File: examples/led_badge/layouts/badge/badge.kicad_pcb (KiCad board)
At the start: 2 copper layers, 56.3 x 38 mm, 237 parts

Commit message: layout tidy up
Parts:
- added U6: , MOLEX_532610271:CONN-SMD_532610271, F.Cu at (121.2, 103.0)
- moved B1 9.35 mm to (96.6, 100.2)
- moved R9 1.01 mm to (115.2, 114.0)
- moved R10 1.01 mm to (115.1, 111.0)
- moved USB1 1.01 mm to (119.7, 112.8)
- moved C111 0.32 mm to (107.2, 103.9)
- moved C4 0.32 mm to (116.1, 103.7)
- moved L1 0.32 mm to (112.7, 107.6)
- moved U2 0.32 mm to (112.6, 104.1)
- moved R1 0.32 mm to (107.9, 107.1)
- moved C110 0.32 mm to (109.0, 103.9)
- moved C112 0.32 mm to (115.3, 107.1)
- moved C3 0.32 mm to (117.9, 103.7)
- moved R2 0.32 mm to (109.2, 107.0)
- moved R3 0.32 mm to (114.5, 100.9)
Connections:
- LED1 pad 4: led_grid-line-0 -> line-11
- LED10 pad 2: led_grid-line-2 -> led_grid-line-1
- LED100 pad 2: led_grid-line-1 -> led_grid-line-0
- LED11 pad 4: led_grid-line-2 -> led_grid-line-1
- LED20 pad 2: led_grid-line-3 -> led_grid-line-2
- LED21 pad 4: led_grid-line-3 -> led_grid-line-2
- LED30 pad 2: led_grid-line-4 -> led_grid-line-3
- LED31 pad 4: led_grid-line-4 -> led_grid-line-3
- LED40 pad 2: led_grid-line-5 -> led_grid-line-4
- LED41 pad 4: led_grid-line-5 -> led_grid-line-4
- LED50 pad 2: led_grid-line-6 -> led_grid-line-5
- LED51 pad 4: led_grid-line-6 -> led_grid-line-5
- LED60 pad 2: led_grid-line-7 -> led_grid-line-6
- LED61 pad 4: led_grid-line-7 -> led_grid-line-6
- LED70 pad 2: led_grid-line-8 -> led_grid-line-7
- LED71 pad 4: led_grid-line-8 -> led_grid-line-7
- LED80 pad 2: led_grid-line-9 -> led_grid-line-8
- LED81 pad 4: led_grid-line-9 -> led_grid-line-8
- LED90 pad 2: led_grid-line-10 -> led_grid-line-9
- LED91 pad 4: led_grid-line-10 -> led_grid-line-9
- U3 pad : (no net) -> mic.package.footprint.pins[0].net-net
- USB1 pad : (no net) -> usb_c.conn.footprint.pins[0].net-net
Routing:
- net led_grid-line-10: track 41.6 -> 0.00 mm, vias 2 -> 0
- net led_grid-line-1: track 0.00 -> 41.3 mm, vias 0 -> 2
- net line-11: track 0.00 -> 0.73 mm, vias 0 -> 1

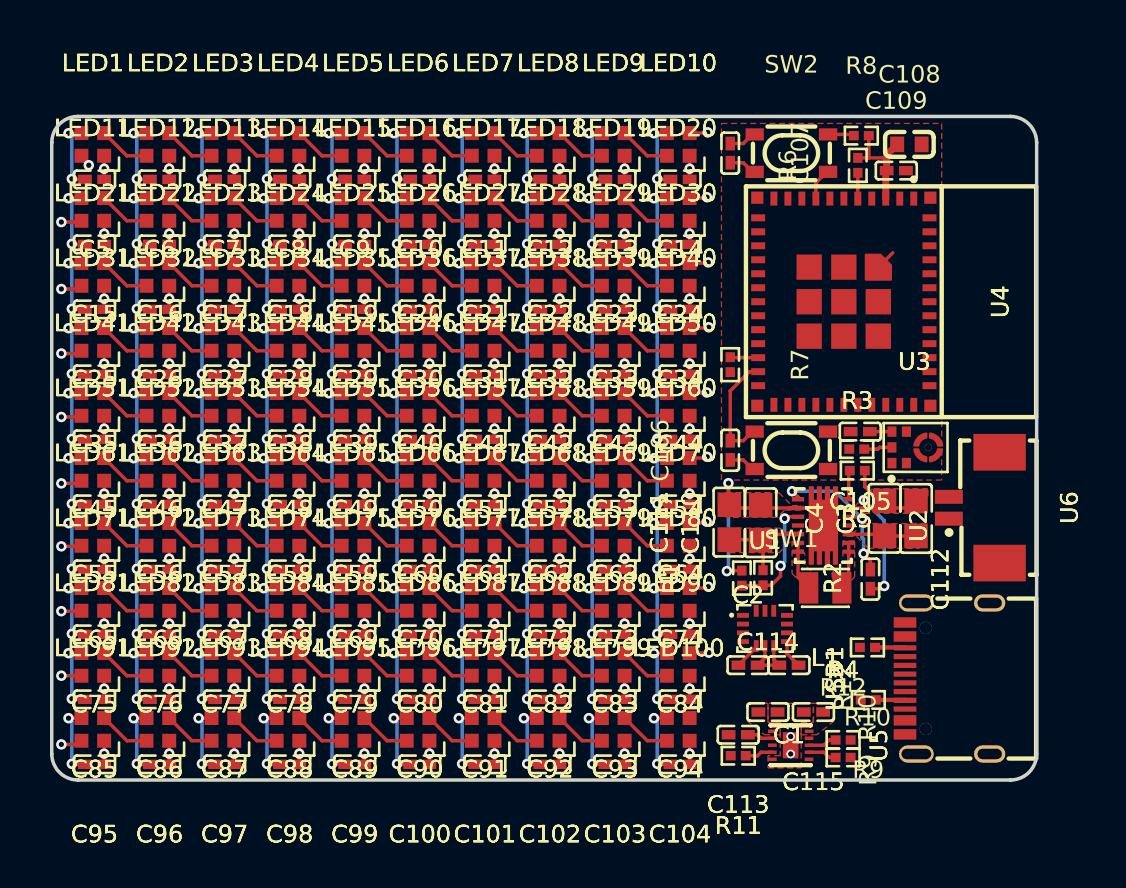
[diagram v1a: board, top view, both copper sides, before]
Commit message: fix 3d models
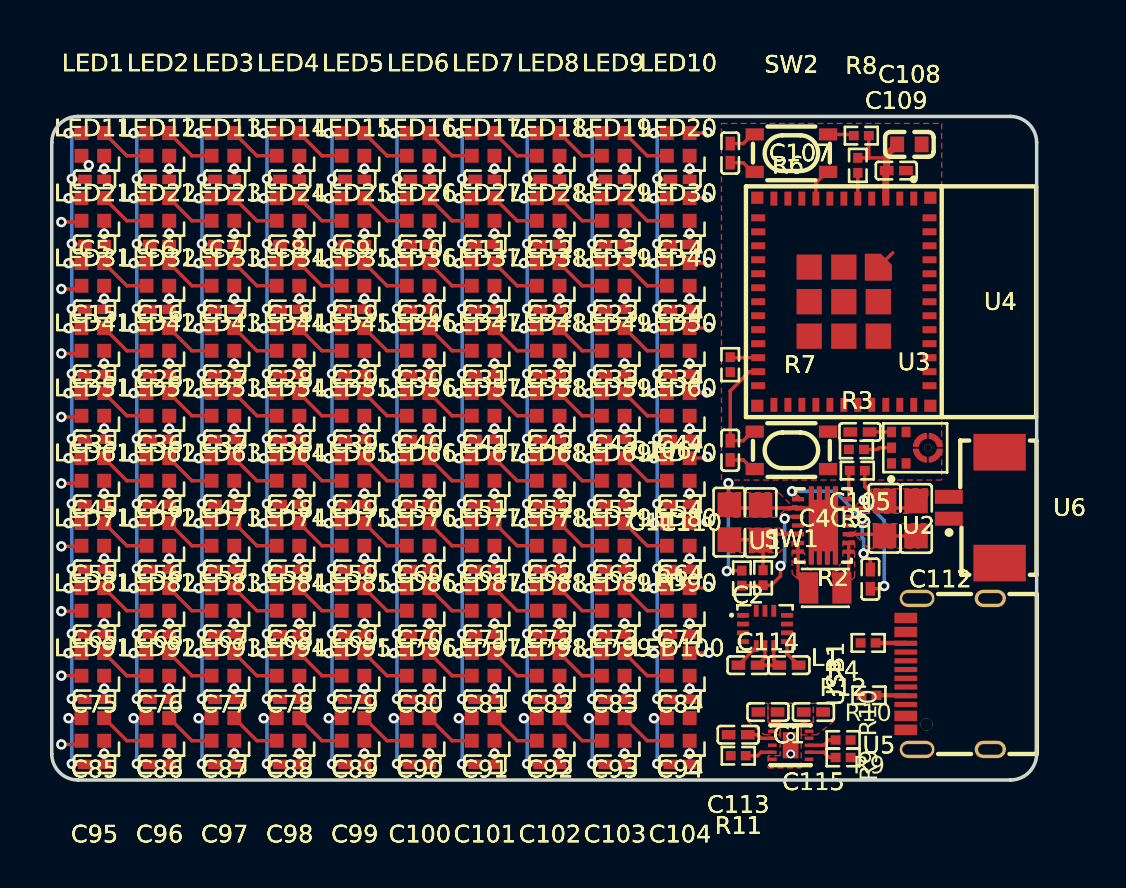
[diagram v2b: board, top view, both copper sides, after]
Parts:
- moved R10 0.26 mm to (115.2, 110.8)
- moved R9 0.26 mm to (115.2, 113.8)
- moved USB1 0.26 mm to (119.7, 112.5)
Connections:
- net mic.package.footprint.pins[0].net-net renamed microphone.package.footprint.pins[0].net-net
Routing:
- removed copper zone on F.Cu, net IN

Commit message: almost complete layout
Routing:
- net line-11: track 0.73 -> 50.8 mm, vias 1 -> 2
- net BAT: track 1.48 -> 29.9 mm, vias 0 -> 4
- net -hv: track 3.90 -> 19.5 mm
- net line-4: track 0.00 -> 15.4 mm, vias 0 -> 2
- net IN: track 0.00 -> 15.3 mm
- net line-3: track 0.00 -> 14.8 mm, vias 0 -> 2
- net hv: track 151.6 -> 164.7 mm, vias 100 -> 112
- net line-5: track 1.62 -> 13.4 mm, vias 0 -> 2
- net gnd: track 453.0 -> 460.1 mm, vias 206 -> 213
- net output-1: track 6.52 -> 10.7 mm
- net output-0: track 3.48 -> 7.68 mm
- net input: track 3.11 -> 7.31 mm
- added copper zone on B.Cu, net gnd
- added copper zone on In1.Cu, net gnd
- added copper zone on In2.Cu, net gnd
- added copper zone on B.Cu, net hv
- added copper zone on In1.Cu, net hv
- added copper zone on In2.Cu, net hv
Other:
- board size 56.3 x 38 mm -> 56.3 x 39 mm
- copper layers 2 -> 4

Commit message: layout ready for final review
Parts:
- added R13: 4.7kΩ ±1% 62.5mW, UNI_ROYAL_0402WGF4701TCE:R0402, F.Cu at (107.2, 90.8)
- added R14: 4.7kΩ ±1% 62.5mW, UNI_ROYAL_0402WGF4701TCE:R0402, F.Cu at (107.2, 92.8)
- added R15: 10kΩ ±1% 62.5mW, UNI_ROYAL_0402WGF1002TCE:R0402, F.Cu at (114.2, 82.2)
- moved R6 23.2 mm to (115.9, 106.6), turned to -90 degrees
- moved R8 15.1 mm to (107.2, 94.8), turned to -90 degrees
- moved R7 15.1 mm to (115.3, 82.2), turned to 90 degrees
- moved B1 2.20 mm to (94.6, 99.2)
- moved C112 0.39 mm to (114.9, 107.2)
- moved U6 0.20 mm to (121.0, 103.0)
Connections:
- net -hv renamed power_sys
- net BAT renamed power_batt
- net line-10 renamed micro-line-6
- net line-12 renamed micro-line-7
- net line-6 renamed micro-line-3
- net line-8 renamed micro-line-4
- net line-9 renamed micro-line-5
- net micro.esp32_module.package.footprint.pins[16].net-net renamed micro.esp32_c3.package.footprint.pins[16].net-net
- net micro.esp32_module.package.footprint.pins[17].net-net renamed micro.esp32_c3.package.footprint.pins[17].net-net
- net micro.esp32_module.package.footprint.pins[1].net-net renamed micro.esp32_c3.package.footprint.pins[1].net-net
- net micro.esp32_module.package.footprint.pins[20].net-net renamed micro.esp32_c3.package.footprint.pins[20].net-net
- net micro.esp32_module.package.footprint.pins[21].net-net renamed micro.esp32_c3.package.footprint.pins[21].net-net
- net micro.esp32_module.package.footprint.pins[25].net-net renamed micro.esp32_c3.package.footprint.pins[25].net-net
- net micro.esp32_module.package.footprint.pins[26].net-net renamed micro.esp32_c3.package.footprint.pins[26].net-net
- net micro.esp32_module.package.footprint.pins[27].net-net renamed micro.esp32_c3.package.footprint.pins[27].net-net
- net micro.esp32_module.package.footprint.pins[28].net-net renamed micro.esp32_c3.package.footprint.pins[28].net-net
- net micro.esp32_module.package.footprint.pins[33].net-net renamed micro.esp32_c3.package.footprint.pins[33].net-net
- net micro.esp32_module.package.footprint.pins[50].net-net renamed micro.esp32_c3.package.footprint.pins[50].net-net
- net micro.esp32_module.package.footprint.pins[52].net-net renamed micro.esp32_c3.package.footprint.pins[52].net-net
- net micro.esp32_module.package.footprint.pins[6].net-net renamed micro.esp32_c3.package.footprint.pins[6].net-net
- net micro.esp32_module.package.footprint.pins[8].net-net renamed micro.esp32_c3.package.footprint.pins[8].net-net
- C1 pad 1: hv -> power_3v3
- C10 pad 1: hv -> power_3v3
- C100 pad 1: hv -> power_3v3
- C101 pad 1: hv -> power_3v3
- C102 pad 1: hv -> power_3v3
- C103 pad 1: hv -> power_3v3
- C104 pad 1: hv -> power_3v3
- C105 pad 1: hv -> power_3v3
- C106 pad 2: output-1 -> output-0
- C107 pad 1: input -> gnd
- C107 pad 2: output-0 -> output-1
- C108 pad 1: hv -> power_3v3
- C109 pad 1: hv -> power_3v3
- C11 pad 1: hv -> power_3v3
- C110 pad 1: hv -> power_3v3
- C111 pad 1: hv -> power_3v3
- C115 pad 1: IN -> usb_power
- C12 pad 1: hv -> power_3v3
- C13 pad 1: hv -> power_3v3
- C14 pad 1: hv -> power_3v3
- C15 pad 1: hv -> power_3v3
- C16 pad 1: hv -> power_3v3
- C17 pad 1: hv -> power_3v3
- C18 pad 1: hv -> power_3v3
- C19 pad 1: hv -> power_3v3
- C2 pad 1: hv -> power_3v3
- C20 pad 1: hv -> power_3v3
- C21 pad 1: hv -> power_3v3
- C22 pad 1: hv -> power_3v3
- C23 pad 1: hv -> power_3v3
- C24 pad 1: hv -> power_3v3
- C25 pad 1: hv -> power_3v3
- C26 pad 1: hv -> power_3v3
- C27 pad 1: hv -> power_3v3
- C28 pad 1: hv -> power_3v3
- C29 pad 1: hv -> power_3v3
- C30 pad 1: hv -> power_3v3
- C31 pad 1: hv -> power_3v3
- C32 pad 1: hv -> power_3v3
- C33 pad 1: hv -> power_3v3
- C34 pad 1: hv -> power_3v3
- C35 pad 1: hv -> power_3v3
- C36 pad 1: hv -> power_3v3
- C37 pad 1: hv -> power_3v3
- C38 pad 1: hv -> power_3v3
- C39 pad 1: hv -> power_3v3
- C40 pad 1: hv -> power_3v3
- C41 pad 1: hv -> power_3v3
- C42 pad 1: hv -> power_3v3
- C43 pad 1: hv -> power_3v3
- C44 pad 1: hv -> power_3v3
- C45 pad 1: hv -> power_3v3
- C46 pad 1: hv -> power_3v3
- C47 pad 1: hv -> power_3v3
- C48 pad 1: hv -> power_3v3
- C49 pad 1: hv -> power_3v3
- C5 pad 1: hv -> power_3v3
- C50 pad 1: hv -> power_3v3
- C51 pad 1: hv -> power_3v3
- C52 pad 1: hv -> power_3v3
- C53 pad 1: hv -> power_3v3
- C54 pad 1: hv -> power_3v3
- C55 pad 1: hv -> power_3v3
- C56 pad 1: hv -> power_3v3
- C57 pad 1: hv -> power_3v3
- C58 pad 1: hv -> power_3v3
- C59 pad 1: hv -> power_3v3
- C6 pad 1: hv -> power_3v3
- C60 pad 1: hv -> power_3v3
- C61 pad 1: hv -> power_3v3
- C62 pad 1: hv -> power_3v3
- C63 pad 1: hv -> power_3v3
- C64 pad 1: hv -> power_3v3
- C65 pad 1: hv -> power_3v3
- C66 pad 1: hv -> power_3v3
- C67 pad 1: hv -> power_3v3
- C68 pad 1: hv -> power_3v3
- C69 pad 1: hv -> power_3v3
- C7 pad 1: hv -> power_3v3
- C70 pad 1: hv -> power_3v3
- C71 pad 1: hv -> power_3v3
- C72 pad 1: hv -> power_3v3
- C73 pad 1: hv -> power_3v3
- C74 pad 1: hv -> power_3v3
- C75 pad 1: hv -> power_3v3
- C76 pad 1: hv -> power_3v3
- C77 pad 1: hv -> power_3v3
- C78 pad 1: hv -> power_3v3
- C79 pad 1: hv -> power_3v3
- C8 pad 1: hv -> power_3v3
- C80 pad 1: hv -> power_3v3
- C81 pad 1: hv -> power_3v3
- C82 pad 1: hv -> power_3v3
- C83 pad 1: hv -> power_3v3
- C84 pad 1: hv -> power_3v3
- C85 pad 1: hv -> power_3v3
- C86 pad 1: hv -> power_3v3
- C87 pad 1: hv -> power_3v3
- C88 pad 1: hv -> power_3v3
- C89 pad 1: hv -> power_3v3
- C9 pad 1: hv -> power_3v3
- C90 pad 1: hv -> power_3v3
- C91 pad 1: hv -> power_3v3
- C92 pad 1: hv -> power_3v3
- C93 pad 1: hv -> power_3v3
- C94 pad 1: hv -> power_3v3
- C95 pad 1: hv -> power_3v3
- C96 pad 1: hv -> power_3v3
- C97 pad 1: hv -> power_3v3
- C98 pad 1: hv -> power_3v3
- C99 pad 1: hv -> power_3v3
- LED1 pad 1: hv -> power_3v3
- LED1 pad 4: line-11 -> led_data
- LED10 pad 1: hv -> power_3v3
- LED100 pad 1: hv -> power_3v3
- LED11 pad 1: hv -> power_3v3
- LED12 pad 1: hv -> power_3v3
- LED13 pad 1: hv -> power_3v3
- LED14 pad 1: hv -> power_3v3
- LED15 pad 1: hv -> power_3v3
- LED16 pad 1: hv -> power_3v3
- LED17 pad 1: hv -> power_3v3
- LED18 pad 1: hv -> power_3v3
- LED19 pad 1: hv -> power_3v3
- LED2 pad 1: hv -> power_3v3
- LED20 pad 1: hv -> power_3v3
- LED21 pad 1: hv -> power_3v3
- LED22 pad 1: hv -> power_3v3
- LED23 pad 1: hv -> power_3v3
- LED24 pad 1: hv -> power_3v3
- LED25 pad 1: hv -> power_3v3
- LED26 pad 1: hv -> power_3v3
- LED27 pad 1: hv -> power_3v3
- LED28 pad 1: hv -> power_3v3
- LED29 pad 1: hv -> power_3v3
- LED3 pad 1: hv -> power_3v3
- LED30 pad 1: hv -> power_3v3
- LED31 pad 1: hv -> power_3v3
- LED32 pad 1: hv -> power_3v3
- LED33 pad 1: hv -> power_3v3
- LED34 pad 1: hv -> power_3v3
- LED35 pad 1: hv -> power_3v3
- LED36 pad 1: hv -> power_3v3
- LED37 pad 1: hv -> power_3v3
- LED38 pad 1: hv -> power_3v3
- LED39 pad 1: hv -> power_3v3
- LED4 pad 1: hv -> power_3v3
- LED40 pad 1: hv -> power_3v3
- LED41 pad 1: hv -> power_3v3
- LED42 pad 1: hv -> power_3v3
- LED43 pad 1: hv -> power_3v3
- LED44 pad 1: hv -> power_3v3
- LED45 pad 1: hv -> power_3v3
- LED46 pad 1: hv -> power_3v3
- LED47 pad 1: hv -> power_3v3
- LED48 pad 1: hv -> power_3v3
- LED49 pad 1: hv -> power_3v3
- LED5 pad 1: hv -> power_3v3
- LED50 pad 1: hv -> power_3v3
- LED51 pad 1: hv -> power_3v3
- LED52 pad 1: hv -> power_3v3
- LED53 pad 1: hv -> power_3v3
- LED54 pad 1: hv -> power_3v3
- LED55 pad 1: hv -> power_3v3
- LED56 pad 1: hv -> power_3v3
- LED57 pad 1: hv -> power_3v3
- LED58 pad 1: hv -> power_3v3
- LED59 pad 1: hv -> power_3v3
- LED6 pad 1: hv -> power_3v3
- LED60 pad 1: hv -> power_3v3
- LED61 pad 1: hv -> power_3v3
- LED62 pad 1: hv -> power_3v3
- LED63 pad 1: hv -> power_3v3
- LED64 pad 1: hv -> power_3v3
- LED65 pad 1: hv -> power_3v3
- LED66 pad 1: hv -> power_3v3
- LED67 pad 1: hv -> power_3v3
- LED68 pad 1: hv -> power_3v3
- LED69 pad 1: hv -> power_3v3
- LED7 pad 1: hv -> power_3v3
- LED70 pad 1: hv -> power_3v3
- LED71 pad 1: hv -> power_3v3
- LED72 pad 1: hv -> power_3v3
- LED73 pad 1: hv -> power_3v3
- LED74 pad 1: hv -> power_3v3
- LED75 pad 1: hv -> power_3v3
- LED76 pad 1: hv -> power_3v3
- LED77 pad 1: hv -> power_3v3
- LED78 pad 1: hv -> power_3v3
- LED79 pad 1: hv -> power_3v3
- LED8 pad 1: hv -> power_3v3
- LED80 pad 1: hv -> power_3v3
- LED81 pad 1: hv -> power_3v3
- LED82 pad 1: hv -> power_3v3
- LED83 pad 1: hv -> power_3v3
- LED84 pad 1: hv -> power_3v3
- LED85 pad 1: hv -> power_3v3
- LED86 pad 1: hv -> power_3v3
- LED87 pad 1: hv -> power_3v3
- LED88 pad 1: hv -> power_3v3
- LED89 pad 1: hv -> power_3v3
- LED9 pad 1: hv -> power_3v3
- LED90 pad 1: hv -> power_3v3
- LED91 pad 1: hv -> power_3v3
- LED92 pad 1: hv -> power_3v3
- LED93 pad 1: hv -> power_3v3
- LED94 pad 1: hv -> power_3v3
- LED95 pad 1: hv -> power_3v3
- LED96 pad 1: hv -> power_3v3
- LED97 pad 1: hv -> power_3v3
- LED98 pad 1: hv -> power_3v3
- LED99 pad 1: hv -> power_3v3
- R2 pad 1: hv -> power_3v3
- R5 pad 1: line-5 -> i2s_sd
- R6 pad 1: line-2 -> EN
- R6 pad 2: hv -> usb_power
- R7 pad 1: line-13 -> micro-line-0
- R7 pad 2: hv -> power_3v3
- R8 pad 1: input -> led_data
- R8 pad 2: hv -> power_3v3
- SW1 pad 3: output-1 -> output-0
- SW1 pad 4: output-1 -> output-0
- SW2 pad 1: input -> gnd
- SW2 pad 2: input -> gnd
- SW2 pad 3: output-0 -> output-1
- SW2 pad 4: output-0 -> output-1
- U1 pad 13: SCL -> i2c_scl
- U1 pad 14: SDA -> i2c_sda
- U1 pad 5: hv -> power_3v3
- U1 pad 8: hv -> power_3v3
- U2 pad 4: hv -> power_3v3
- U2 pad 5: hv -> power_3v3
- U3 pad 1: line-4 -> i2s_ws
- U3 pad 4: line-3 -> i2s_sck
- U3 pad 5: hv -> power_3v3
- U3 pad 6: line-5 -> i2s_sd
- U4 pad 12: line-0 -> i2s_sck
- U4 pad 13: line-1 -> i2s_sd
- U4 pad 18: line-4 -> micro-line-2
- U4 pad 19: line-5 -> i2c_sda
- U4 pad 20: line-11 -> i2c_scl
- U4 pad 22: line-13 -> led_data
- U4 pad 23: output-1 -> output-0
- U4 pad 26: line-7 -> i2s_ws
- U4 pad 3: hv -> power_3v3
- U4 pad 5: line-2 -> micro-line-0
- U4 pad 6: line-3 -> micro-line-1
- U4 pad 8: output-0 -> output-1
- U5 pad 10: IN -> usb_power
- USB1 pad A4: IN -> usb_power
- USB1 pad A9: IN -> usb_power
- USB1 pad B4: IN -> usb_power
- USB1 pad B9: IN -> usb_power
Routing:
- net power_3v3: track 0.00 -> 171.4 mm, vias 0 -> 112
- net hv: track 164.7 -> 0.00 mm, vias 112 -> 0
- net led_data: track 0.00 -> 53.2 mm
- net line-11: track 50.8 -> 0.00 mm, vias 2 -> 0
- net i2c_sda: track 0.00 -> 23.0 mm, vias 0 -> 2
- net usb_power: track 0.00 -> 21.9 mm, vias 0 -> 2
- net i2c_scl: track 0.00 -> 21.4 mm, vias 0 -> 2
- net i2s_sd: track 0.00 -> 17.8 mm, vias 0 -> 2
- net gnd: track 460.1 -> 477.7 mm, vias 213 -> 218
- net i2s_sck: track 0.00 -> 17.3 mm, vias 0 -> 2
- net line-4: track 15.4 -> 0.00 mm, vias 2 -> 0
- net IN: track 15.3 -> 0.00 mm
- net line-3: track 14.8 -> 0.00 mm, vias 2 -> 0
- net line-5: track 13.4 -> 0.00 mm, vias 2 -> 0
- net i2s_ws: track 0.00 -> 11.9 mm, vias 0 -> 2
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- added copper zone on B.Cu, net power_3v3
- added copper zone on F.Cu, net power_3v3
- added copper zone on In2.Cu, net power_3v3
- removed copper zone on In1.Cu, net gnd
- removed copper zone on In2.Cu, net gnd
- removed copper zone on B.Cu, net hv
- removed copper zone on F.Cu, net hv
- removed copper zone on In1.Cu, net hv
- removed copper zone on In2.Cu, net hv

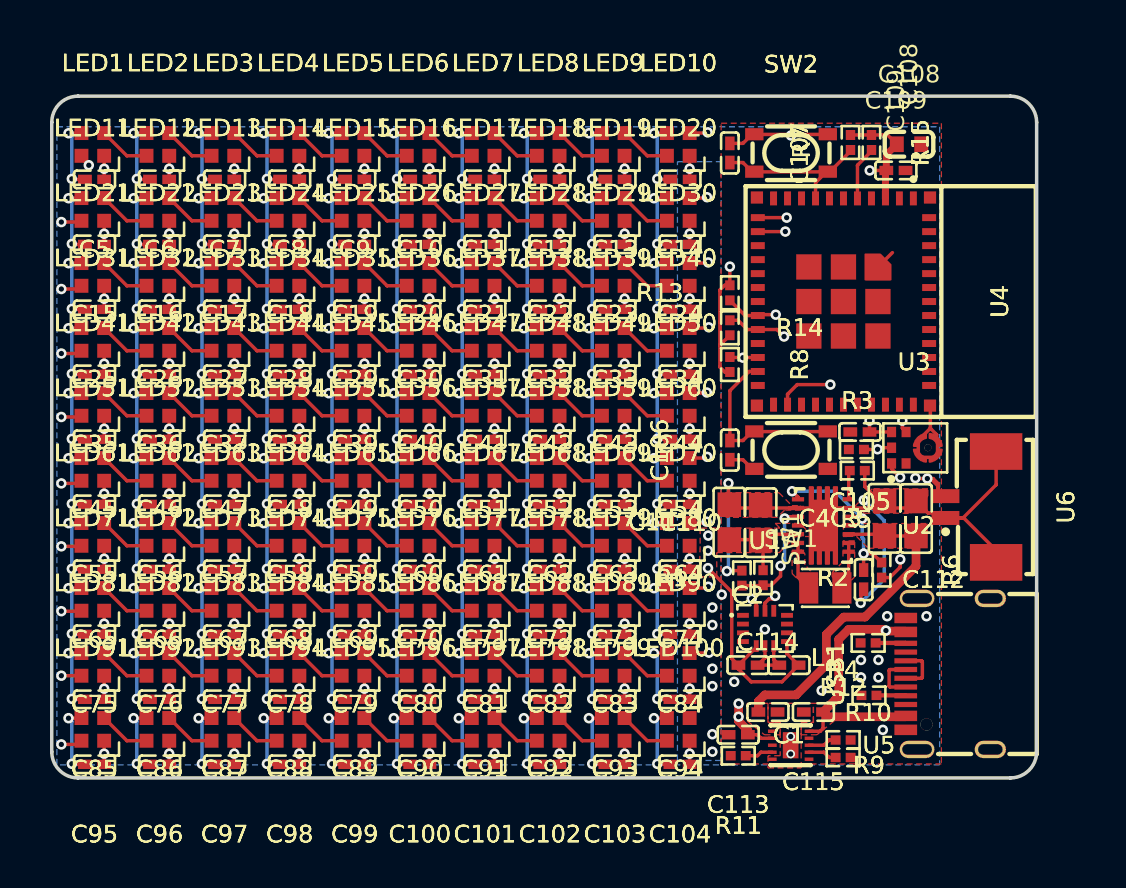
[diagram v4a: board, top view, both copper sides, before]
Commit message: Fix: copper pour, usb data, usb connector hole, keepout zone, add logo
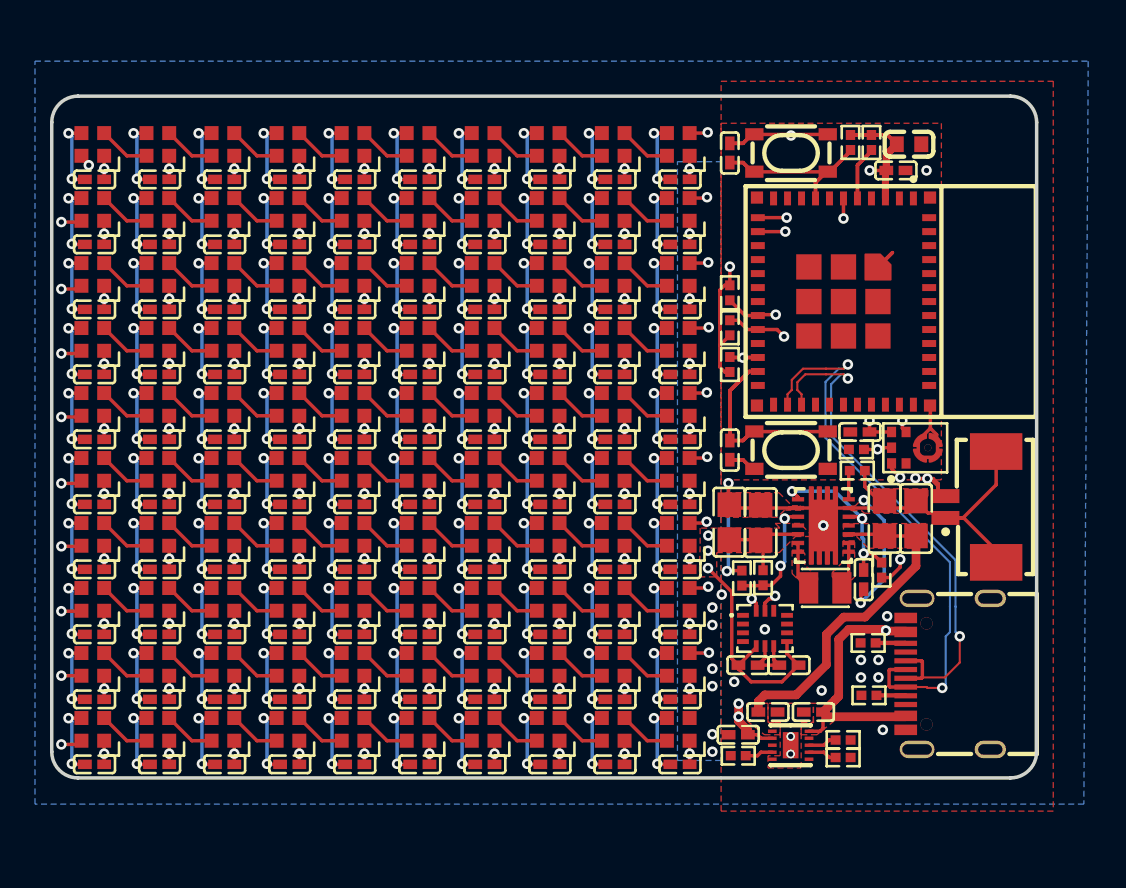
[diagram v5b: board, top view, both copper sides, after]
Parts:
- added LOGO1: , atopile_Logo_8x8mm:atopile_Logo_8x8mm, B.Cu at (119.5, 85.2)
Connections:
- net micro-line-0 renamed microcontroller-line-0
- net micro-line-2 renamed microcontroller-line-1
- net micro-line-3 renamed microcontroller-line-2
- net micro-line-5 renamed microcontroller-line-3
- net micro-line-6 renamed microcontroller-line-4
- net micro-line-7 renamed microcontroller-line-5
- net micro.esp32_c3.package.footprint.pins[16].net-net renamed microcontroller.esp32_c3.package.footprint.pins[16].net-net
- net micro.esp32_c3.package.footprint.pins[17].net-net renamed microcontroller.esp32_c3.package.footprint.pins[17].net-net
- net micro.esp32_c3.package.footprint.pins[1].net-net renamed microcontroller.esp32_c3.package.footprint.pins[1].net-net
- net micro.esp32_c3.package.footprint.pins[20].net-net renamed microcontroller.esp32_c3.package.footprint.pins[20].net-net
- net micro.esp32_c3.package.footprint.pins[21].net-net renamed microcontroller.esp32_c3.package.footprint.pins[21].net-net
- net micro.esp32_c3.package.footprint.pins[25].net-net renamed microcontroller.esp32_c3.package.footprint.pins[25].net-net
- net micro.esp32_c3.package.footprint.pins[26].net-net renamed microcontroller.esp32_c3.package.footprint.pins[26].net-net
- net micro.esp32_c3.package.footprint.pins[27].net-net renamed microcontroller.esp32_c3.package.footprint.pins[27].net-net
- net micro.esp32_c3.package.footprint.pins[28].net-net renamed microcontroller.esp32_c3.package.footprint.pins[28].net-net
- net micro.esp32_c3.package.footprint.pins[33].net-net renamed microcontroller.esp32_c3.package.footprint.pins[33].net-net
- net micro.esp32_c3.package.footprint.pins[50].net-net renamed microcontroller.esp32_c3.package.footprint.pins[50].net-net
- net micro.esp32_c3.package.footprint.pins[52].net-net renamed microcontroller.esp32_c3.package.footprint.pins[52].net-net
- net micro.esp32_c3.package.footprint.pins[6].net-net renamed microcontroller.esp32_c3.package.footprint.pins[6].net-net
- net micro.esp32_c3.package.footprint.pins[8].net-net renamed microcontroller.esp32_c3.package.footprint.pins[8].net-net
- U4 pad 26: i2s_ws -> usb_N
- U4 pad 27: micro-line-4 -> usb_P
- U4 pad 6: micro-line-1 -> i2s_ws
- USB1 pad A6: A6 -> usb_P
- USB1 pad A7: A7 -> usb_N
- USB1 pad B6: A6 -> usb_P
- USB1 pad B7: A7 -> usb_N
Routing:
- net usb_N: track 0.00 -> 32.4 mm, vias 0 -> 2
- net usb_P: track 0.00 -> 30.2 mm, vias 0 -> 2
- net i2s_ws: track 11.9 -> 19.3 mm
- net output-0: track 10.7 -> 17.2 mm
- net power_3v3: track 171.4 -> 177.6 mm
- net output-1: track 9.53 -> 14.9 mm
- net gnd: track 477.7 -> 482.1 mm, vias 218 -> 219
- net microcontroller-line-0: track 3.10 -> 6.20 mm
- net A7: track 2.84 -> 0.00 mm
- net A6: track 2.84 -> 0.00 mm
- net led_data: track 53.2 -> 54.9 mm, vias 0 -> 2
- net (no net): vias 2 -> 0
